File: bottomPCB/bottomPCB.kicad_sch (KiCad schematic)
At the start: 41 parts, among them J1 Conn_01x03_Pin, U1 ESP32-WROOM-32, U2 XT30_horizontal, U8 LM1117IMPX-3_3_NOPB, U9 LM1117IMPX-3_3_NOPB

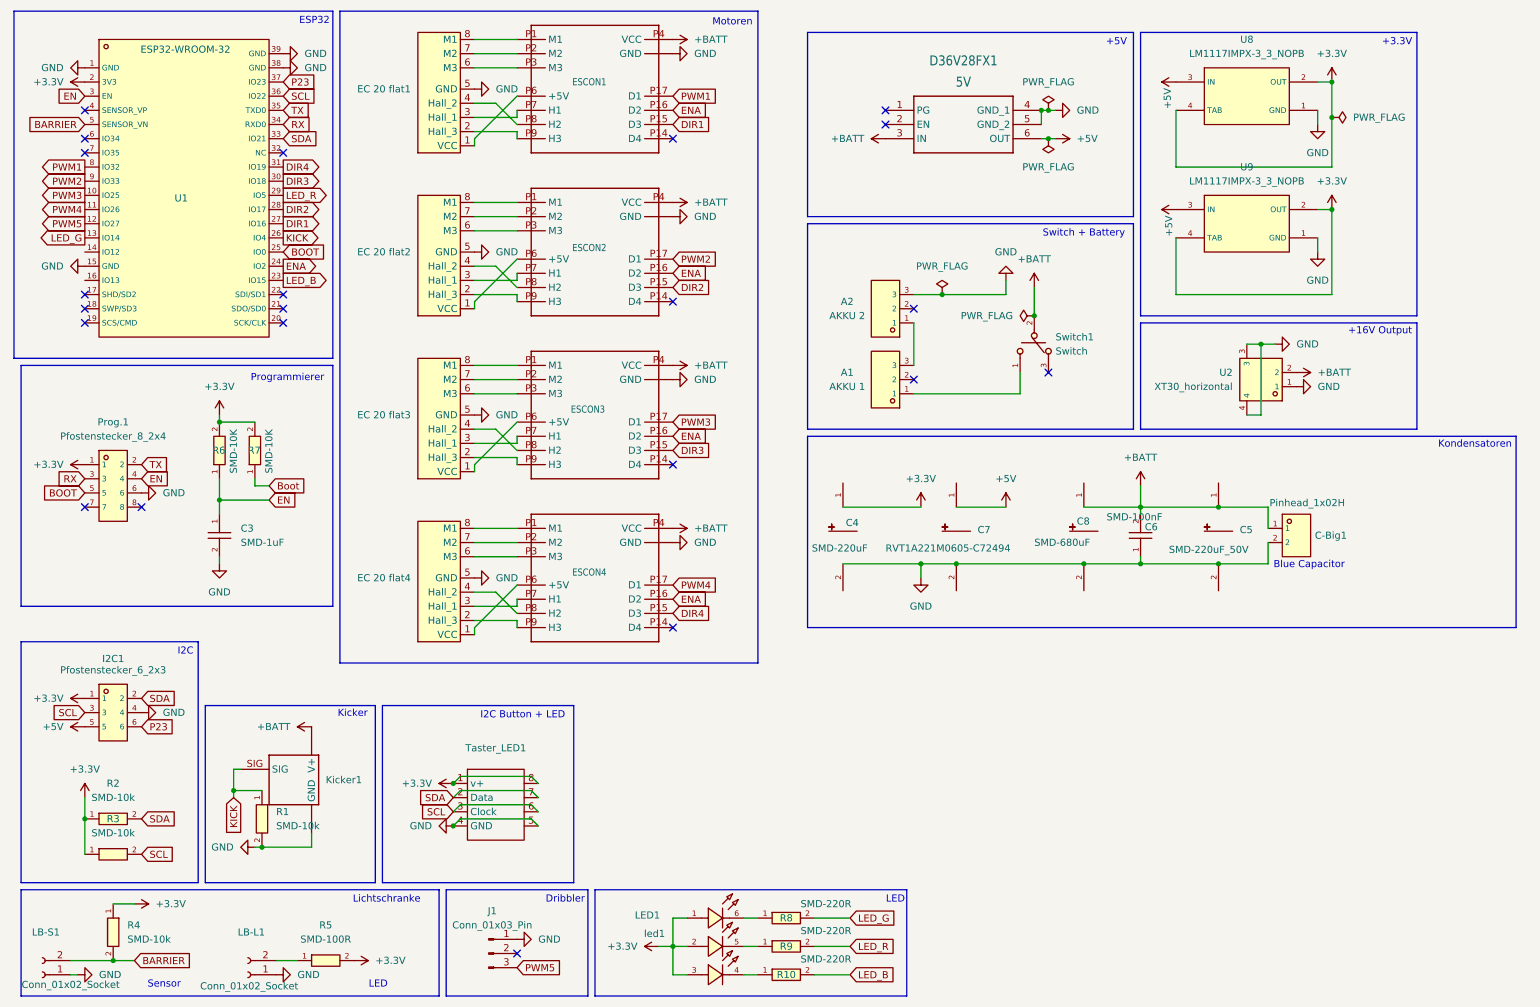
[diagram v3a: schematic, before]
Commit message: added 3 Pullup-Input pins and 2 GPIO pins
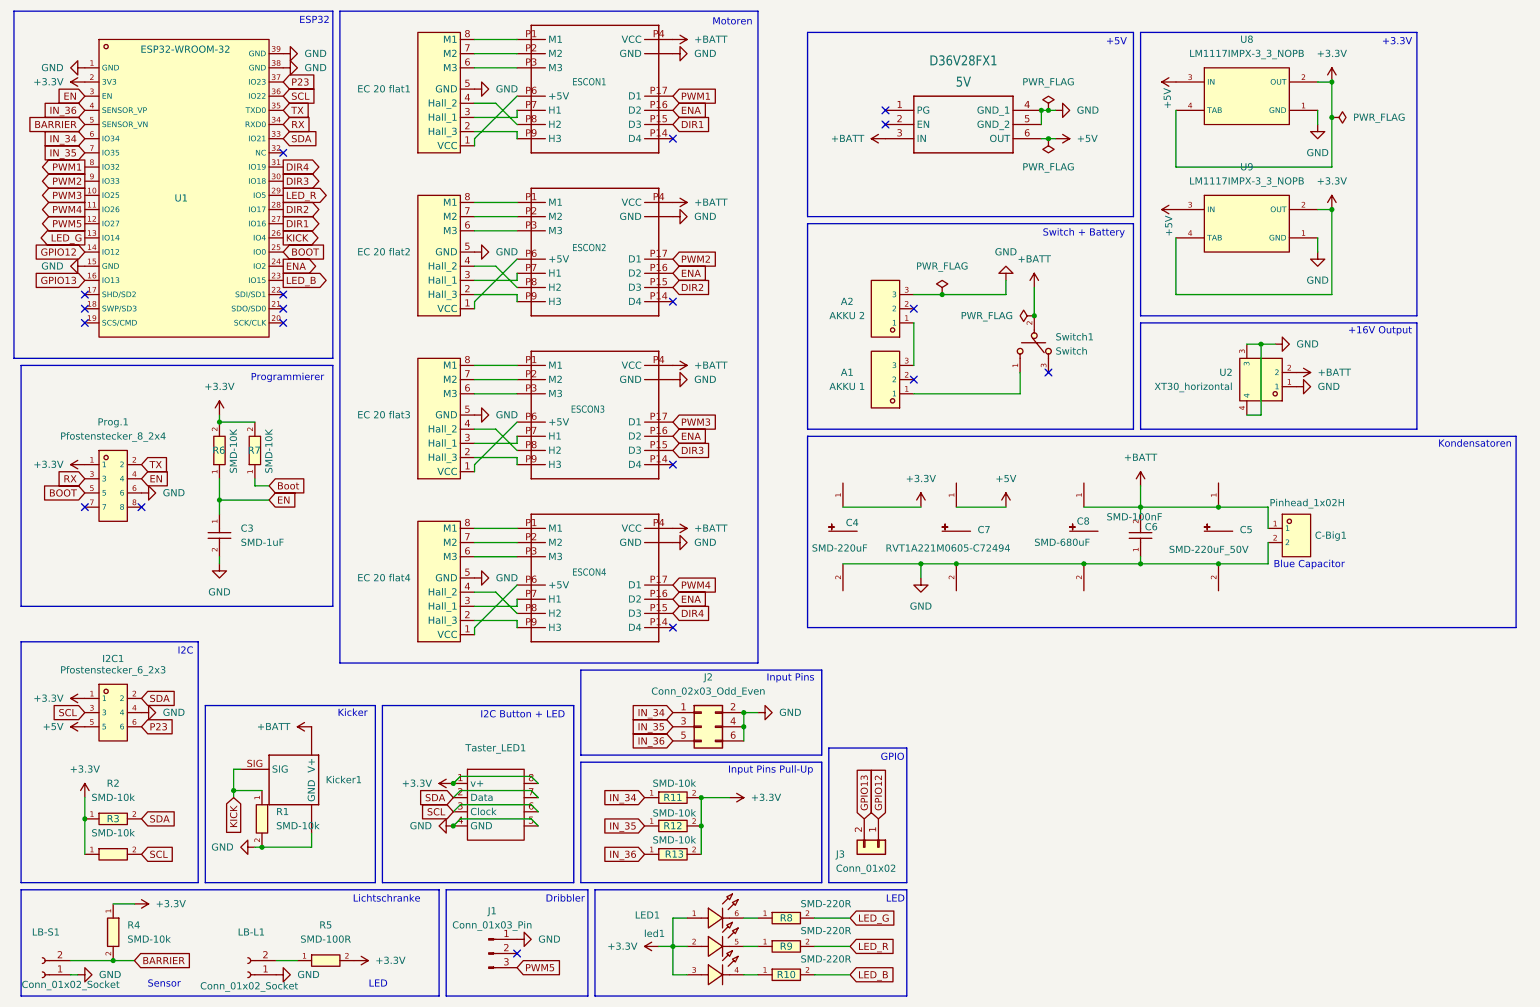
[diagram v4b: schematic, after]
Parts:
- added J2: Conn_02x03_Odd_Even, symbol Connector_Generic:Conn_02x03_Odd_Even
- added J3: Conn_01x02, symbol Connector_Generic:Conn_01x02
- added R11, R12, R13: SMD-10k, BohleBots:R0603, symbol bohlebots.lib:SMD-10k
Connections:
- net +3.3V: now also R11.2, R12.2, R13.2
- net GND: now also J2.2 (Pin_2), J2.4 (Pin_4), J2.6 (Pin_6)
- net GPIO12: now reaches U1.14 (IO12)
- net GPIO12: now also J3.1 (Pin_1)
- net GPIO13: now reaches U1.16 (IO13)
- net GPIO13: now also J3.2 (Pin_2)
- net IN_36: now reaches U1.4 (SENSOR_VP)
- net IN_36: now also J2.5 (Pin_5), R13.1
- net IN_34: now reaches U1.6 (IO34)
- net IN_34: now also J2.1 (Pin_1), R11.1
- net IN_35: now reaches U1.7 (IO35)
- net IN_35: now also J2.3 (Pin_3), R12.1
- no-connect marks 22 -> 19
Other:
- note added: "GPIO"
- note added: "Input Pins"
- note added: "Input Pins Pull-Up"

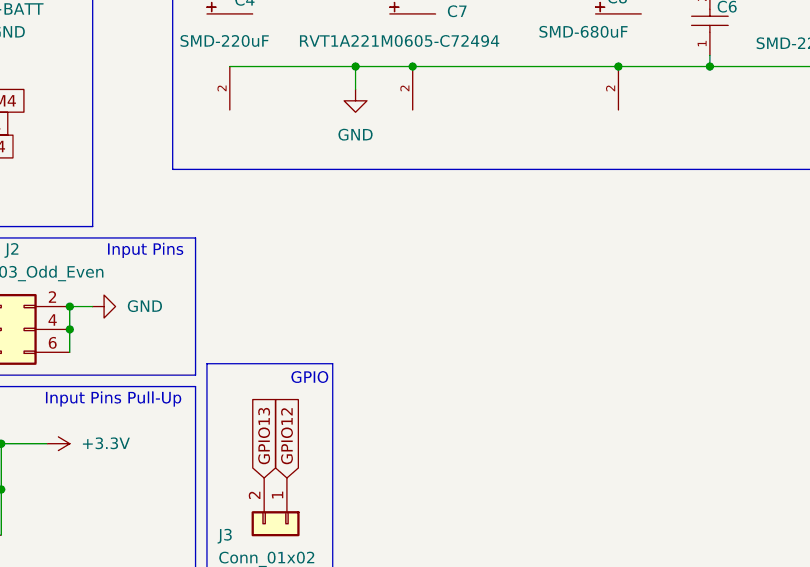
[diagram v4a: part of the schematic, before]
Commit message: added power pins
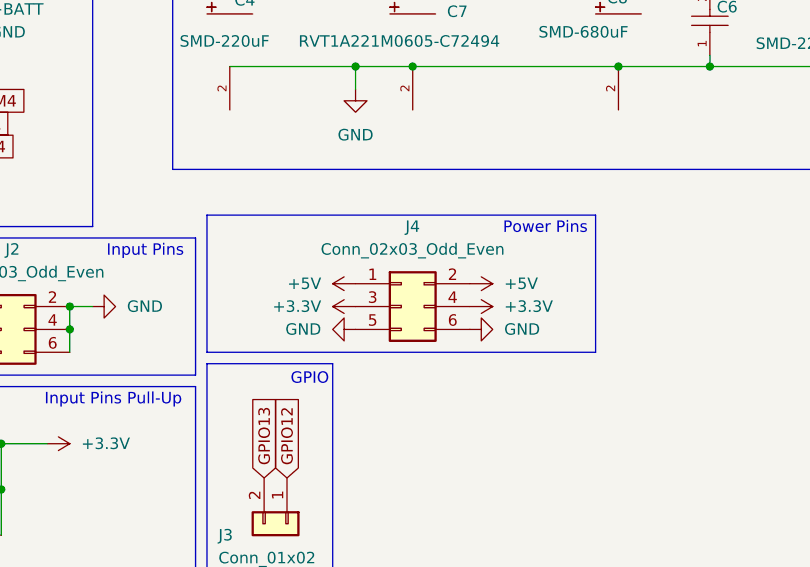
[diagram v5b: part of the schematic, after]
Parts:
- added J4: Conn_02x03_Odd_Even, symbol Connector_Generic:Conn_02x03_Odd_Even
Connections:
- net +3.3V: now also J4.3 (Pin_3), J4.4 (Pin_4)
- net +5V: now also J4.1 (Pin_1), J4.2 (Pin_2)
- net GND: now also J4.5 (Pin_5), J4.6 (Pin_6)
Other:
- note added: "Power Pins"

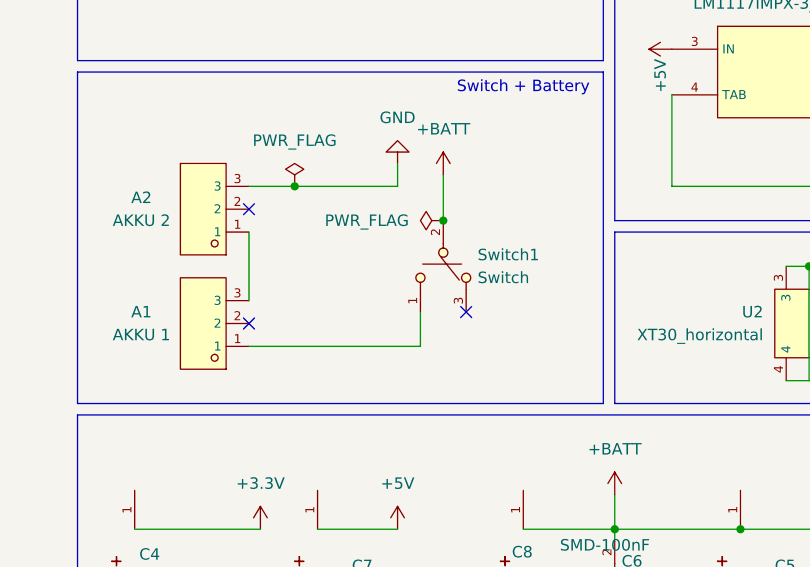
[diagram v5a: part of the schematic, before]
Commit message: WIP: removed switch
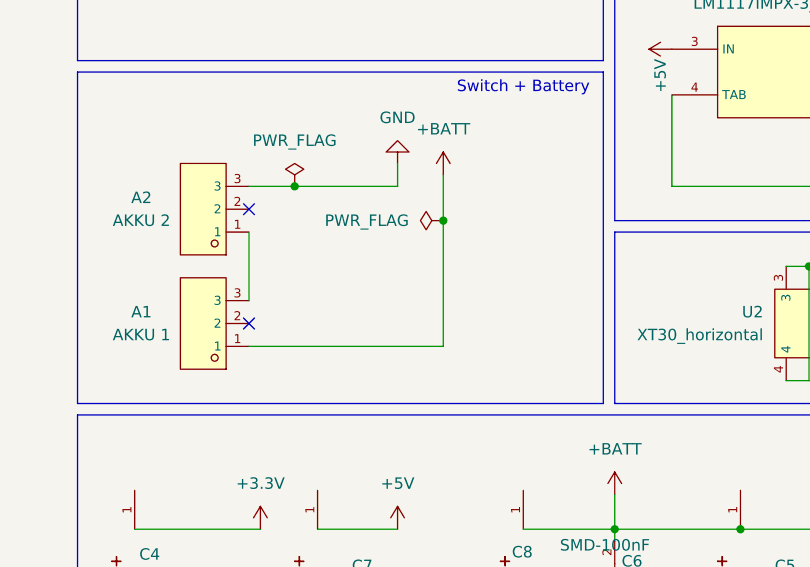
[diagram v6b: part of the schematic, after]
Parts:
- removed Switch1: Switch, BohleBots:SW-TH_MT-0-103-A101-M200-RS, symbol bohlebots.lib:Switch
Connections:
- net +BATT: now also A1.1
- no-connect marks 19 -> 18
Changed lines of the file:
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@@
 	)
 	(junction
-		(at 195.58 67.31)
+		(at 214.63 111.76)
 		(diameter 0)
 		(color 0 0 0 0)
 	)
 	(junction
-		(at 214.63 111.76)
+		(at 49.53 100.33)
 		(diameter 0)
 		(color 0 0 0 0)
 	)
 	(junction
-		(at 49.53 100.33)
+		(at 91.44 151.13)
 		(diameter 0)
 		(color 0 0 0 0)
 	)
 	(junction
-		(at 91.44 151.13)
+		(at 195.58 67.31)
 		(diameter 0)
 		(color 0 0 0 0)
@@
 	)
 	(no_connect
-		(at 198.12 77.47)
-	)
-	(no_connect
 		(at 35.56 101.6)
 	)
@@
 	(wire
 		(pts
+			(xy 195.58 67.31) (xy 195.58 81.28)
+		)
+		(stroke
+			(width 0)
+			(type default)
+		)
+	)
+	(wire
+		(pts
 			(xy 49.53 111.76) (xy 49.53 110.49)
 		)
@@
 	(wire
 		(pts
-			(xy 173.99 81.28) (xy 193.04 81.28)
+			(xy 173.99 81.28) (xy 195.58 81.28)
 		)
 		(stroke
@@
 	(wire
 		(pts
-			(xy 193.04 77.47) (xy 193.04 81.28)
-		)
-		(stroke
-			(width 0)
-			(type default)
-		)
-	)
-	(wire
-		(pts
 			(xy 156.21 175.26) (xy 162.56 175.26)
 		)
@@
 					(unit 1)
 				)
-			)
-		)
-	)
-	(symbol
-		(lib_id "bohlebots.lib:Switch")
-		(at 195.58 72.39 0)
-		(unit 1)
-		(exclude_from_sim no)
-		(in_bom yes)
-		(on_board yes)
-		(dnp no)
-		(fields_autoplaced yes)
-		(property "Reference" "Switch1"
-			(at 199.39 71.1199 0)
-			(effects
-				(font
-					(size 1.27 1.27)
-				)
-				(justify left)
-			)
-		)
-		(property "Value" "Switch"
-			(at 199.39 73.6599 0)
-			(effects
-				(font
-					(size 1.27 1.27)
-				)
-				(justify left)
-			)
-		)
-		(property "Footprint" "BohleBots:SW-TH_MT-0-103-A101-M200-RS"
-			(at 195.58 82.55 0)
-			(effects
-				(font
-					(size 1.27 1.27)
-					(italic yes)
-				)
-				(hide yes)
-			)
-		)
-		(property "Datasheet" "https://item.szlcsc.com/1879284.html"
-			(at 193.294 72.263 0)
-			(effects
-				(font
-					(size 1.27 1.27)
-				)
-				(justify left)
-				(hide yes)
-			)
-		)
-		(property "Description" ""
-			(at 195.58 72.39 0)
-			(effects
-				(font
-					(size 1.27 1.27)
-				)
-				(hide yes)
-			)
-		)
-		(property "LCSC" "C1788498"
-			(at 195.58 72.39 0)
-			(effects
-				(font
-					(size 1.27 1.27)
-				)
-				(hide yes)
-			)
-		)
-		(pin "1"
-		)
-		(pin "2"
-		)
-		(pin "3"
-		)
-		(instances
-			(project "bottomPCB"
-				(path "/530b96b6-d439-440e-a48e-82f0fe8f4bb1"
-					(reference "Switch1")
-					(unit 1)
-				)

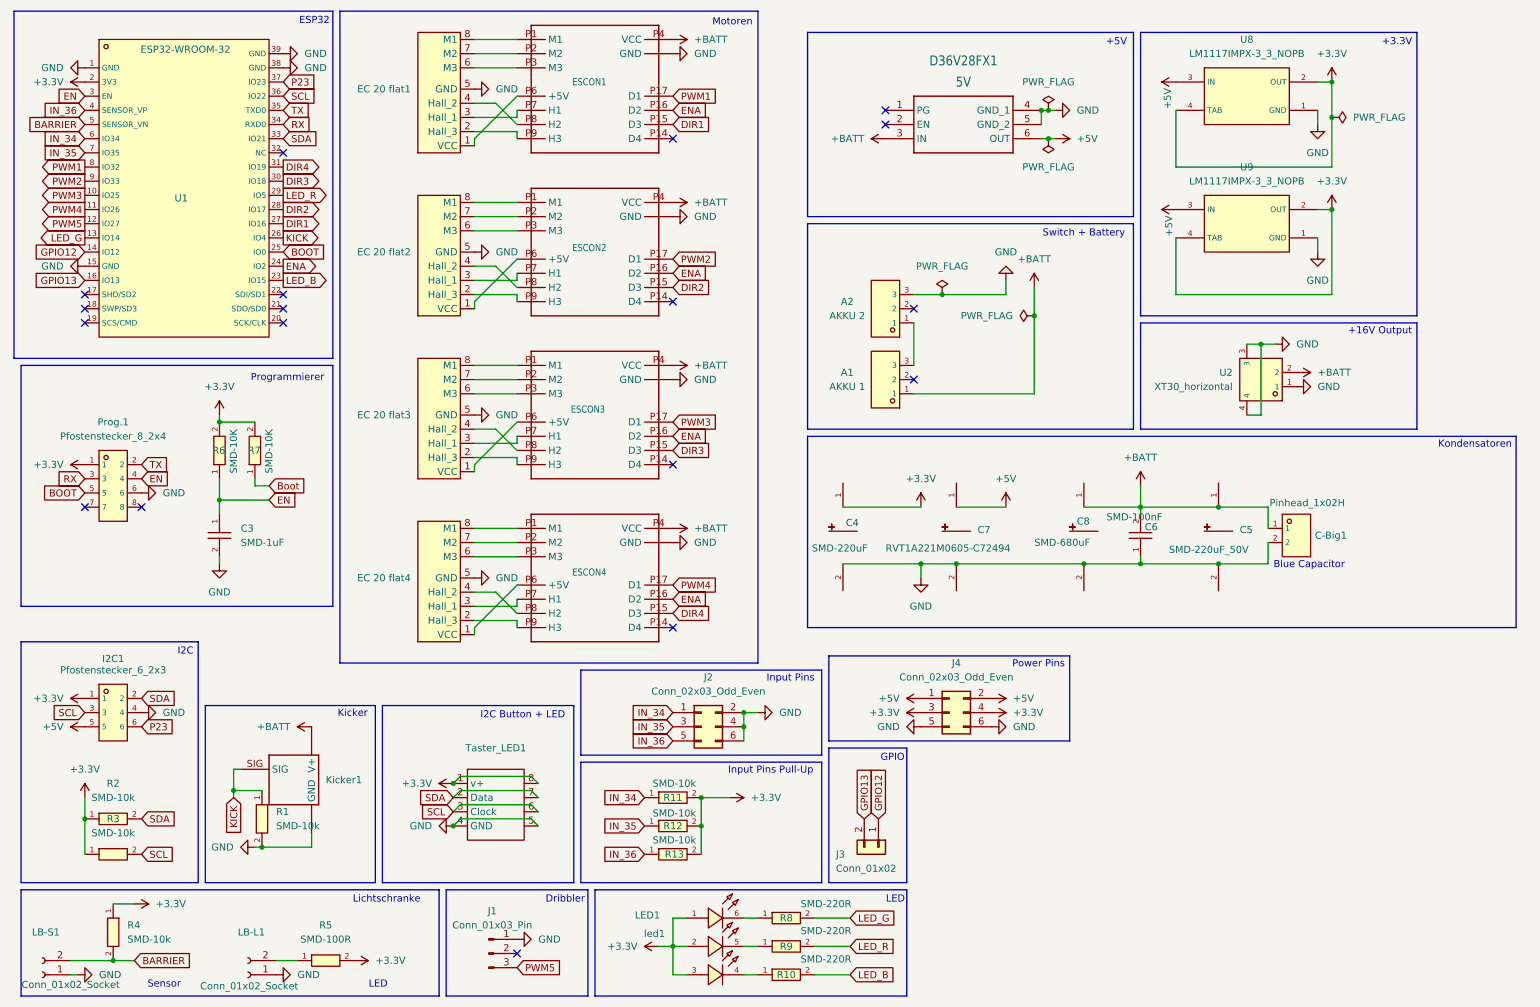
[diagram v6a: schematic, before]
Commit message: connected ec 20 flat connectors to esp32
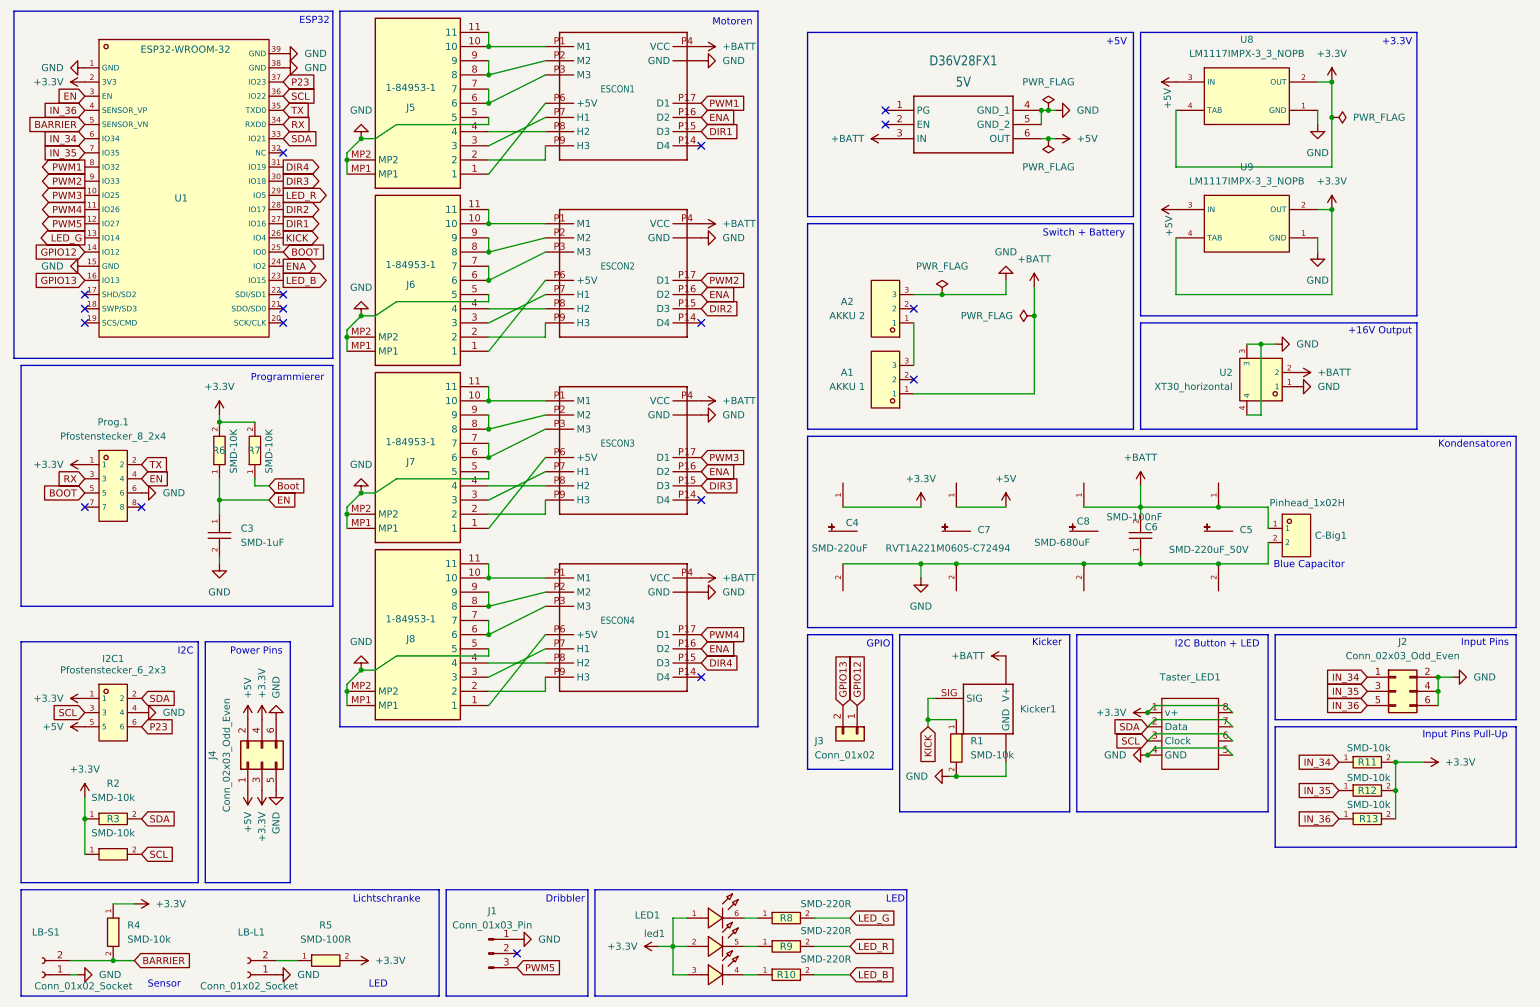
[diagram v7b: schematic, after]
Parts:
- removed EC 20 flat1: ~, symbol EC-20-flat:EC-20-flat
- removed EC 20 flat2: ~, symbol EC-20-flat:EC-20-flat
- removed EC 20 flat3: ~, symbol EC-20-flat:EC-20-flat
- removed EC 20 flat4: ~, symbol EC-20-flat:EC-20-flat
- added J5, J6, J7, J8: 1-84953-1, 1-84953-1:1849531, symbol 1-84953-1:1-84953-1
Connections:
- net GND: now also J5.5, J5.MP1, J5.MP2, J6.5, J6.MP1, J6.MP2, J7.5, J7.MP1, J7.MP2, J8.5, J8.MP1, J8.MP2
- net at ESCON2.P1 (M1): now also J6.10, J6.11
- net at ESCON2.P2 (M2): now also J6.8, J6.9
- net at ESCON2.P3 (M3): now also J6.6, J6.7
- net at ESCON2.P6 (+5V): now also J6.1
- net at ESCON2.P7 (H1): now also J6.3
- net at ESCON2.P8 (H2): now also J6.4
- net at ESCON2.P9 (H3): now also J6.2
- net at ESCON1.P6 (+5V): now also J5.1
- net at ESCON1.P9 (H3): now also J5.2
- net at ESCON1.P7 (H1): now also J5.3
- net at ESCON1.P8 (H2): now also J5.4
- net at ESCON1.P3 (M3): now also J5.6, J5.7
- net at ESCON1.P2 (M2): now also J5.8, J5.9
- net at ESCON1.P1 (M1): now also J5.10, J5.11
- net at ESCON3.P6 (+5V): now also J7.1
- net at ESCON3.P9 (H3): now also J7.2
- net at ESCON3.P7 (H1): now also J7.3
- net at ESCON3.P8 (H2): now also J7.4
- net at ESCON3.P3 (M3): now also J7.6, J7.7
- net at ESCON3.P2 (M2): now also J7.8, J7.9
- net at ESCON3.P1 (M1): now also J7.10, J7.11
- net at ESCON4.P6 (+5V): now also J8.1
- net at ESCON4.P9 (H3): now also J8.2
- net at ESCON4.P7 (H1): now also J8.3
- net at ESCON4.P8 (H2): now also J8.4
- net at ESCON4.P3 (M3): now also J8.6, J8.7
- net at ESCON4.P2 (M2): now also J8.8, J8.9
- net at ESCON4.P1 (M1): now also J8.10, J8.11
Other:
- moved on the sheet: ESCON1, J2, J3, J4, Kicker1, R1, R11, R12, R13, Taster_LED1
